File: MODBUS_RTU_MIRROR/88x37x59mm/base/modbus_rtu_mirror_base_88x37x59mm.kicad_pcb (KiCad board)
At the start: 2 copper layers, 82 x 31 mm, 4 parts

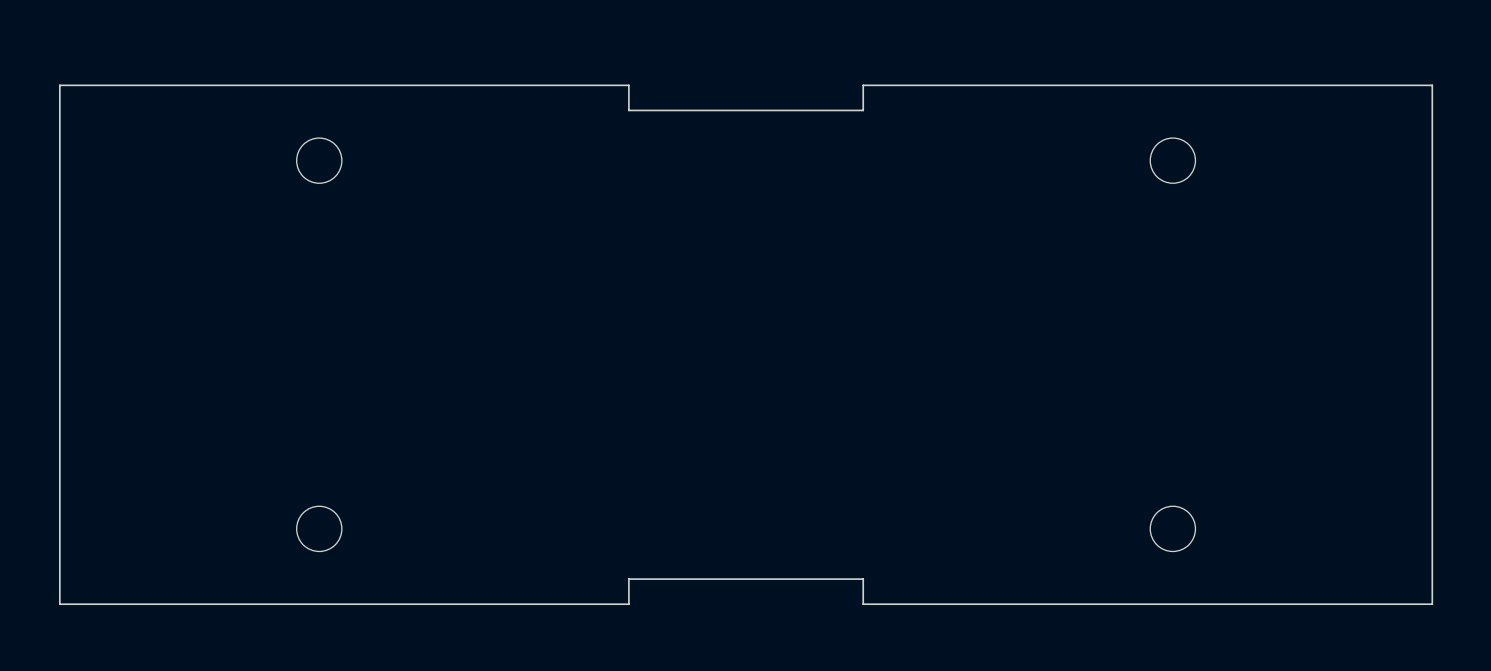
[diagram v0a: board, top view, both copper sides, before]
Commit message: enlarged holes, started putting some components
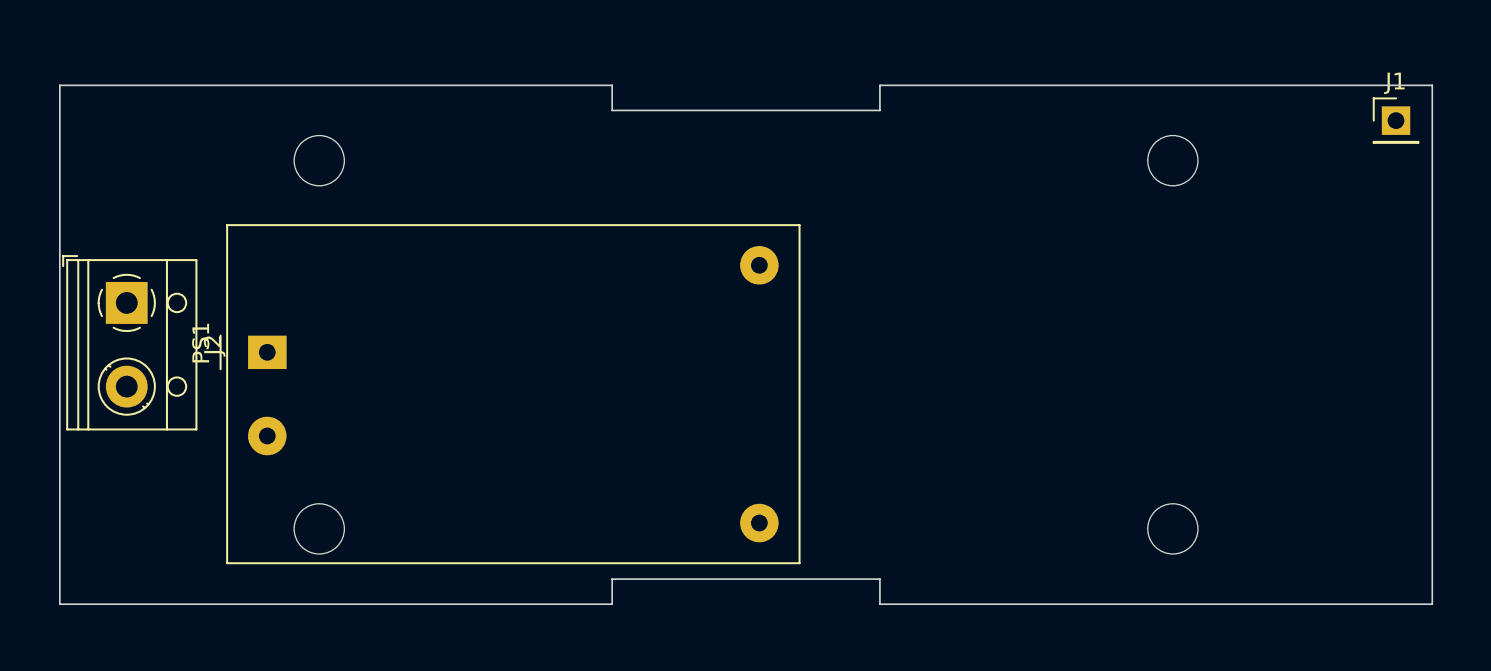
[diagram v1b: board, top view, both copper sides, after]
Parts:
- removed the REF** at (115.5, 126.5)
- removed the REF** at (166.5, 104.5)
- removed the REF** at (166.5, 126.5)
- removed the REF** at (115.5, 104.5)
- added J1: Conn_01x01_Male, Connector_PinHeader_2.54mm:PinHeader_1x01_P2.54mm_Vertical, F.Cu at (179.8, 102.1)
- added J2: Conn_01x02_Female, TerminalBlock_RND:TerminalBlock_RND_205-00012_1x02_P5.00mm_Horizontal, F.Cu at (104.0, 113.0)
- added PS1: HLK-PM01, Converter_ACDC:Converter_ACDC_HiLink_HLK-PMxx, F.Cu at (112.4, 116.0)
- added REF**: MountingHole_3mm, MountingHole:MountingHole_3mm, F.Cu at (166.5, 126.5)
- added REF**: MountingHole_3mm, MountingHole:MountingHole_3mm, F.Cu at (166.5, 104.5)
- added REF**: MountingHole_3mm, MountingHole:MountingHole_3mm, F.Cu at (115.5, 104.5)
- added REF**: MountingHole_3mm, MountingHole:MountingHole_3mm, F.Cu at (115.5, 126.5)
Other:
- outline, holes or cut-outs redrawn

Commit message: added RS485 terminals
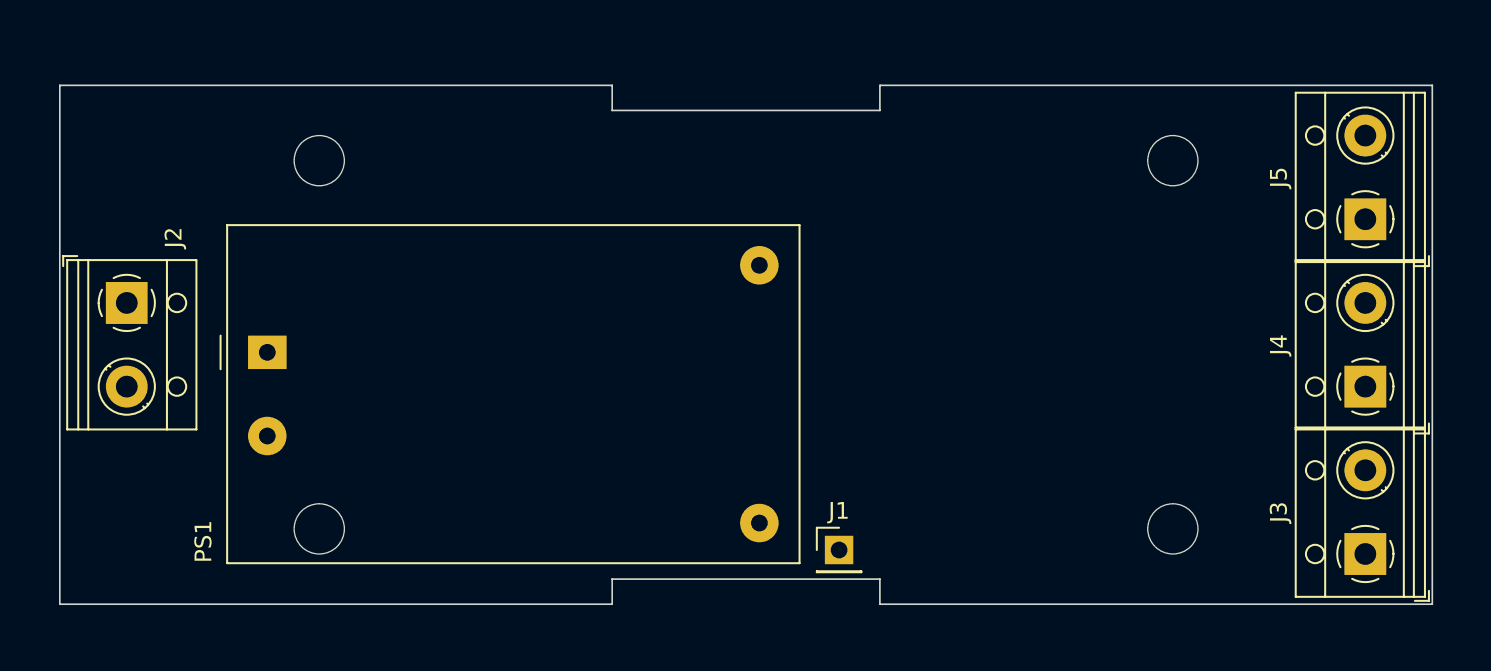
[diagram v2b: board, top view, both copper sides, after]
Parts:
- added J3: Conn_01x02_Female, TerminalBlock_RND:TerminalBlock_RND_205-00012_1x02_P5.00mm_Horizontal, F.Cu at (178.0, 128.0)
- added J4: Conn_01x02_Female, TerminalBlock_RND:TerminalBlock_RND_205-00012_1x02_P5.00mm_Horizontal, F.Cu at (178.0, 118.0)
- added J5: Conn_01x02_Female, TerminalBlock_RND:TerminalBlock_RND_205-00012_1x02_P5.00mm_Horizontal, F.Cu at (178.0, 108.0)
- moved J1 42.0 mm to (146.6, 127.8)

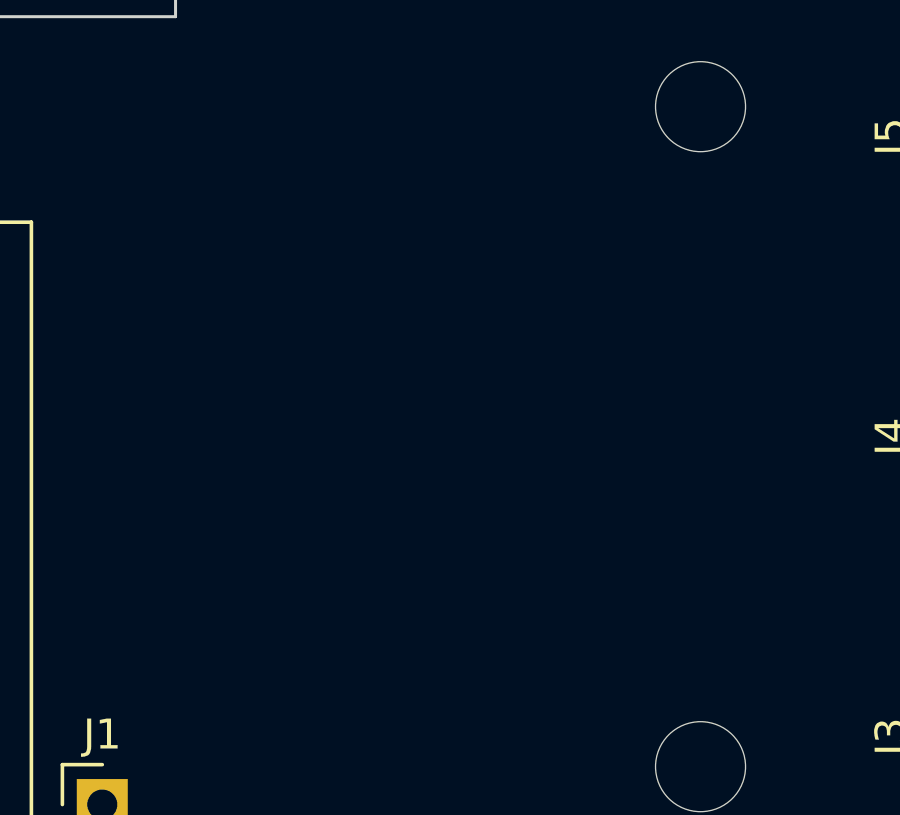
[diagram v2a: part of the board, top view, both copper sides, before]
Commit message: addes 2x rs485 chip
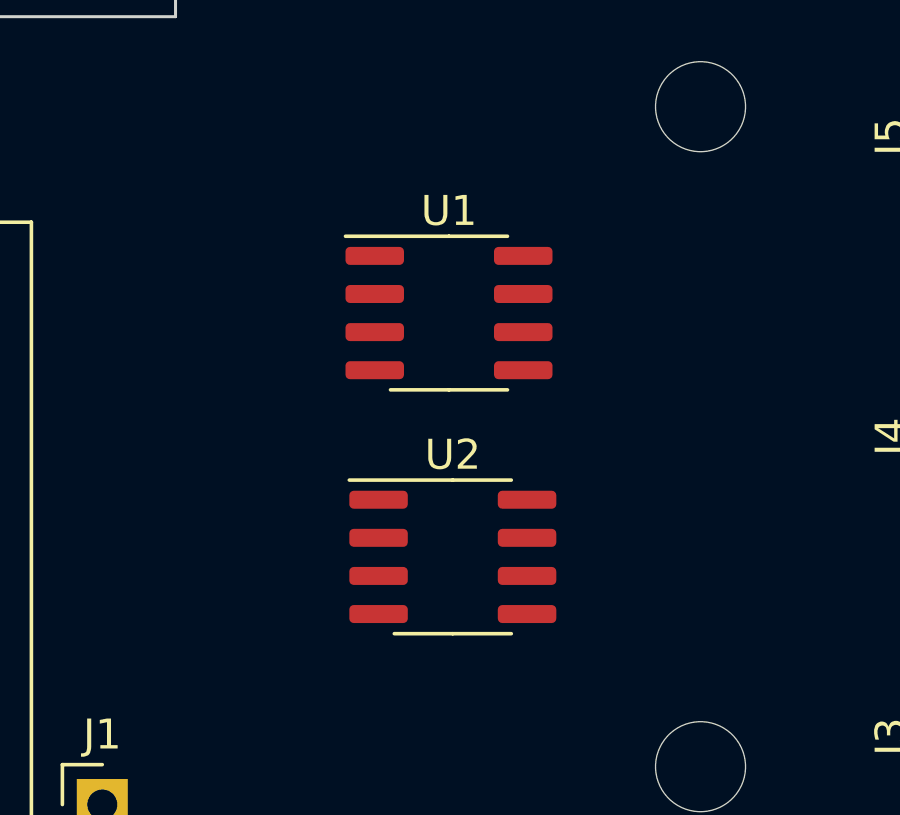
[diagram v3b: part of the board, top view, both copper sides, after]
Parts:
- added U1: ST485EBDR, Package_SO:SOIC-8_3.9x4.9mm_P1.27mm, F.Cu at (158.1, 111.4)
- added U2: ST485EBDR, Package_SO:SOIC-8_3.9x4.9mm_P1.27mm, F.Cu at (158.2, 119.5)
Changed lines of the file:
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@@
   (net 12 "unconnected-(J5-Pad1)")
   (net 13 "unconnected-(J5-Pad2)")
+  (net 14 "unconnected-(U1-Pad1)")
+  (net 15 "unconnected-(U1-Pad2)")
+  (net 16 "unconnected-(U1-Pad3)")
+  (net 17 "unconnected-(U1-Pad4)")
+  (net 18 "unconnected-(U1-Pad5)")
+  (net 19 "unconnected-(U1-Pad6)")
+  (net 20 "unconnected-(U1-Pad7)")
+  (net 21 "unconnected-(U1-Pad8)")
+  (net 22 "unconnected-(U2-Pad1)")
+  (net 23 "unconnected-(U2-Pad2)")
+  (net 24 "unconnected-(U2-Pad3)")
+  (net 25 "unconnected-(U2-Pad4)")
+  (net 26 "unconnected-(U2-Pad5)")
+  (net 27 "unconnected-(U2-Pad6)")
+  (net 28 "unconnected-(U2-Pad7)")
+  (net 29 "unconnected-(U2-Pad8)")
   (footprint "TerminalBlock_RND:TerminalBlock_RND_205-00012_1x02_P5.00mm_Horizontal" (layer "F.Cu")
     (at 178 118 90)
@@
     )
   )
+  (footprint "Package_SO:SOIC-8_3.9x4.9mm_P1.27mm" (layer "F.Cu")
+    (at 158.115 111.379)
+    (descr "SOIC, 8 Pin (JEDEC MS-012AA, https://www.analog.com/media/en/package-pcb-resources/package/pkg_pdf/soic_narrow-r/r_8.pdf), generated with kicad-footprint-generator ipc_gullwing_generator.py")
+    (tags "SOIC SO")
+    (property "Sheetfile" "modbus_rtu_mirror_base_88x37x59mm.kicad_sch")
+    (property "Sheetname" "")
+    (attr smd)
+    (fp_text reference "U1" (at 0 -3.4) (layer "F.SilkS")
+      (effects (font (size 1 1) (thickness 0.15)))
+    )
+    (fp_text value "ST485EBDR" (at 0 3.4) (layer "F.Fab")
+      (effects (font (size 1 1) (thickness 0.15)))
+    )
+    (fp_text user "${REFERENCE}" (at 0 0) (layer "F.Fab")
+      (effects (font (size 0.98 0.98) (thickness 0.15)))
+    )
+    (fp_line (start 0 -2.56) (end -3.45 -2.56) (layer "F.SilkS") (width 0.12))
+    (fp_line (start 0 -2.56) (end 1.95 -2.56) (layer "F.SilkS") (width 0.12))
+    (fp_line (start 0 2.56) (end -1.95 2.56) (layer "F.SilkS") (width 0.12))
+    (fp_line (start 0 2.56) (end 1.95 2.56) (layer "F.SilkS") (width 0.12))
+    (fp_line (start -3.7 2.7) (end 3.7 2.7) (layer "F.CrtYd") (width 0.05))
+    (fp_line (start 3.7 -2.7) (end -3.7 -2.7) (layer "F.CrtYd") (width 0.05))
+    (fp_line (start -3.7 -2.7) (end -3.7 2.7) (layer "F.CrtYd") (width 0.05))
+    (fp_line (start 3.7 2.7) (end 3.7 -2.7) (layer "F.CrtYd") (width 0.05))
+    (fp_line (start 1.95 2.45) (end -1.95 2.45) (layer "F.Fab") (width 0.1))
+    (fp_line (start -1.95 2.45) (end -1.95 -1.475) (layer "F.Fab") (width 0.1))
+    (fp_line (start 1.95 -2.45) (end 1.95 2.45) (layer "F.Fab") (width 0.1))
+    (fp_line (start -1.95 -1.475) (end -0.975 -2.45) (layer "F.Fab") (width 0.1))
+    (fp_line (start -0.975 -2.45) (end 1.95 -2.45) (layer "F.Fab") (width 0.1))
+    (pad "1" smd roundrect (at -2.475 -1.905) (size 1.95 0.6) (layers "F.Cu" "F.Paste" "F.Mask") (roundrect_rratio 0.25)
+      (net 14 "unconnected-(U1-Pad1)") (pinfunction "RO") (pintype "output"))
+    (pad "2" smd roundrect (at -2.475 -0.635) (size 1.95 0.6) (layers "F.Cu" "F.Paste" "F.Mask") (roundrect_rratio 0.25)
+      (net 15 "unconnected-(U1-Pad2)") (pinfunction "~{RE}") (pintype "input"))
+    (pad "3" smd roundrect (at -2.475 0.635) (size 1.95 0.6) (layers "F.Cu" "F.Paste" "F.Mask") (roundrect_rratio 0.25)
+      (net 16 "unconnected-(U1-Pad3)") (pinfunction "DE") (pintype "input"))
+    (pad "4" smd roundrect (at -2.475 1.905) (size 1.95 0.6) (layers "F.Cu" "F.Paste" "F.Mask") (roundrect_rratio 0.25)
+      (net 17 "unconnected-(U1-Pad4)") (pinfunction "DI") (pintype "input"))
+    (pad "5" smd roundrect (at 2.475 1.905) (size 1.95 0.6) (layers "F.Cu" "F.Paste" "F.Mask") (roundrect_rratio 0.25)
+      (net 18 "unconnected-(U1-Pad5)") (pinfunction "GND") (pintype "power_in"))
+    (pad "6" smd roundrect (at 2.475 0.635) (size 1.95 0.6) (layers "F.Cu" "F.Paste" "F.Mask") (roundrect_rratio 0.25)
+      (net 19 "unconnected-(U1-Pad6)") (pinfunction "A") (pintype "bidirectional"))
+    (pad "7" smd roundrect (at 2.475 -0.635) (size 1.95 0.6) (layers "F.Cu" "F.Paste" "F.Mask") (roundrect_rratio 0.25)
+      (net 20 "unconnected-(U1-Pad7)") (pinfunction "B") (pintype "bidirectional"))
+    (pad "8" smd roundrect (at 2.475 -1.905) (size 1.95 0.6) (layers "F.Cu" "F.Paste" "F.Mask") (roundrect_rratio 0.25)
+      (net 21 "unconnected-(U1-Pad8)") (pinfunction "VCC") (pintype "power_in"))
+    (model "${KICAD6_3DMODEL_DIR}/Package_SO.3dshapes/SOIC-8_3.9x4.9mm_P1.27mm.wrl"
+      (offset (xyz 0 0 0))
+      (scale (xyz 1 1 1))
+      (rotate (xyz 0 0 0))
+    )
+  )
   (footprint "TerminalBlock_RND:TerminalBlock_RND_205-00012_1x02_P5.00mm_Horizontal" (layer "F.Cu")
     (at 178 128 90)
@@
       (offset (xyz 0 0 0))
       (scale (xyz 1 1 1))
+      (rotate (xyz 0 0 0))
+    )
+  )
+  (footprint "Package_SO:SOIC-8_3.9x4.9mm_P1.27mm" (layer "F.Cu")
+    (at 158.242 119.507)
+    (descr "SOIC, 8 Pin (JEDEC MS-012AA, https://www.analog.com/media/en/package-pcb-resources/package/pkg_pdf/soic_narrow-r/r_8.pdf), generated with kicad-footprint-generator ipc_gullwing_generator.py")
+    (tags "SOIC SO")
+    (property "Sheetfile" "modbus_rtu_mirror_base_88x37x59mm.kicad_sch")
+    (property "Sheetname" "")
+    (attr smd)
+    (fp_text reference "U2" (at 0 -3.4) (layer "F.SilkS")
+      (effects (font (size 1 1) (thickness 0.15)))
+    )
+    (fp_text value "ST485EBDR" (at 0 3.4) (layer "F.Fab")
+      (effects (font (size 1 1) (thickness 0.15)))
+    )
+    (fp_text user "${REFERENCE}" (at 0 0) (layer "F.Fab")
+      (effects (font (size 0.98 0.98) (thickness 0.15)))
+    )
+    (fp_line (start 0 -2.56) (end -3.45 -2.56) (layer "F.SilkS") (width 0.12))
+    (fp_line (start 0 2.56) (end 1.95 2.56) (layer "F.SilkS") (width 0.12))
+    (fp_line (start 0 -2.56) (end 1.95 -2.56) (layer "F.SilkS") (width 0.12))
+    (fp_line (start 0 2.56) (end -1.95 2.56) (layer "F.SilkS") (width 0.12))
+    (fp_line (start 3.7 2.7) (end 3.7 -2.7) (layer "F.CrtYd") (width 0.05))
+    (fp_line (start -3.7 -2.7) (end -3.7 2.7) (layer "F.CrtYd") (width 0.05))
+    (fp_line (start -3.7 2.7) (end 3.7 2.7) (layer "F.CrtYd") (width 0.05))
+    (fp_line (start 3.7 -2.7) (end -3.7 -2.7) (layer "F.CrtYd") (width 0.05))
+    (fp_line (start -1.95 -1.475) (end -0.975 -2.45) (layer "F.Fab") (width 0.1))
+    (fp_line (start -1.95 2.45) (end -1.95 -1.475) (layer "F.Fab") (width 0.1))
+    (fp_line (start -0.975 -2.45) (end 1.95 -2.45) (layer "F.Fab") (width 0.1))
+    (fp_line (start 1.95 2.45) (end -1.95 2.45) (layer "F.Fab") (width 0.1))
+    (fp_line (start 1.95 -2.45) (end 1.95 2.45) (layer "F.Fab") (width 0.1))
+    (pad "1" smd roundrect (at -2.475 -1.905) (size 1.95 0.6) (layers "F.Cu" "F.Paste" "F.Mask") (roundrect_rratio 0.25)
+      (net 22 "unconnected-(U2-Pad1)") (pinfunction "RO") (pintype "output"))
+    (pad "2" smd roundrect (at -2.475 -0.635) (size 1.95 0.6) (layers "F.Cu" "F.Paste" "F.Mask") (roundrect_rratio 0.25)
+      (net 23 "unconnected-(U2-Pad2)") (pinfunction "~{RE}") (pintype "input"))
+    (pad "3" smd roundrect (at -2.475 0.635) (size 1.95 0.6) (layers "F.Cu" "F.Paste" "F.Mask") (roundrect_rratio 0.25)
+      (net 24 "unconnected-(U2-Pad3)") (pinfunction "DE") (pintype "input"))
+    (pad "4" smd roundrect (at -2.475 1.905) (size 1.95 0.6) (layers "F.Cu" "F.Paste" "F.Mask") (roundrect_rratio 0.25)
+      (net 25 "unconnected-(U2-Pad4)") (pinfunction "DI") (pintype "input"))
+    (pad "5" smd roundrect (at 2.475 1.905) (size 1.95 0.6) (layers "F.Cu" "F.Paste" "F.Mask") (roundrect_rratio 0.25)
+      (net 26 "unconnected-(U2-Pad5)") (pinfunction "GND") (pintype "power_in"))
+    (pad "6" smd roundrect (at 2.475 0.635) (size 1.95 0.6) (layers "F.Cu" "F.Paste" "F.Mask") (roundrect_rratio 0.25)
+      (net 27 "unconnected-(U2-Pad6)") (pinfunction "A") (pintype "bidirectional"))
+    (pad "7" smd roundrect (at 2.475 -0.635) (size 1.95 0.6) (layers "F.Cu" "F.Paste" "F.Mask") (roundrect_rratio 0.25)
+      (net 28 "unconnected-(U2-Pad7)") (pinfunction "B") (pintype "bidirectional"))
+    (pad "8" smd roundrect (at 2.475 -1.905) (size 1.95 0.6) (layers "F.Cu" "F.Paste" "F.Mask") (roundrect_rratio 0.25)
+      (net 29 "unconnected-(U2-Pad8)") (pinfunction "VCC") (pintype "power_in"))
+    (model "${KICAD6_3DMODEL_DIR}/Package_SO.3dshapes/SOIC-8_3.9x4.9mm_P1.27mm.wrl"
+      (offset (xyz 0 0 0))
+      (scale (xyz 1 1 1))
